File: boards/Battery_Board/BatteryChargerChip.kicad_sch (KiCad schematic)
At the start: 11 parts, among them J103 Conn_01x02, Q1 PMOS, U1 BQ25185DLHR

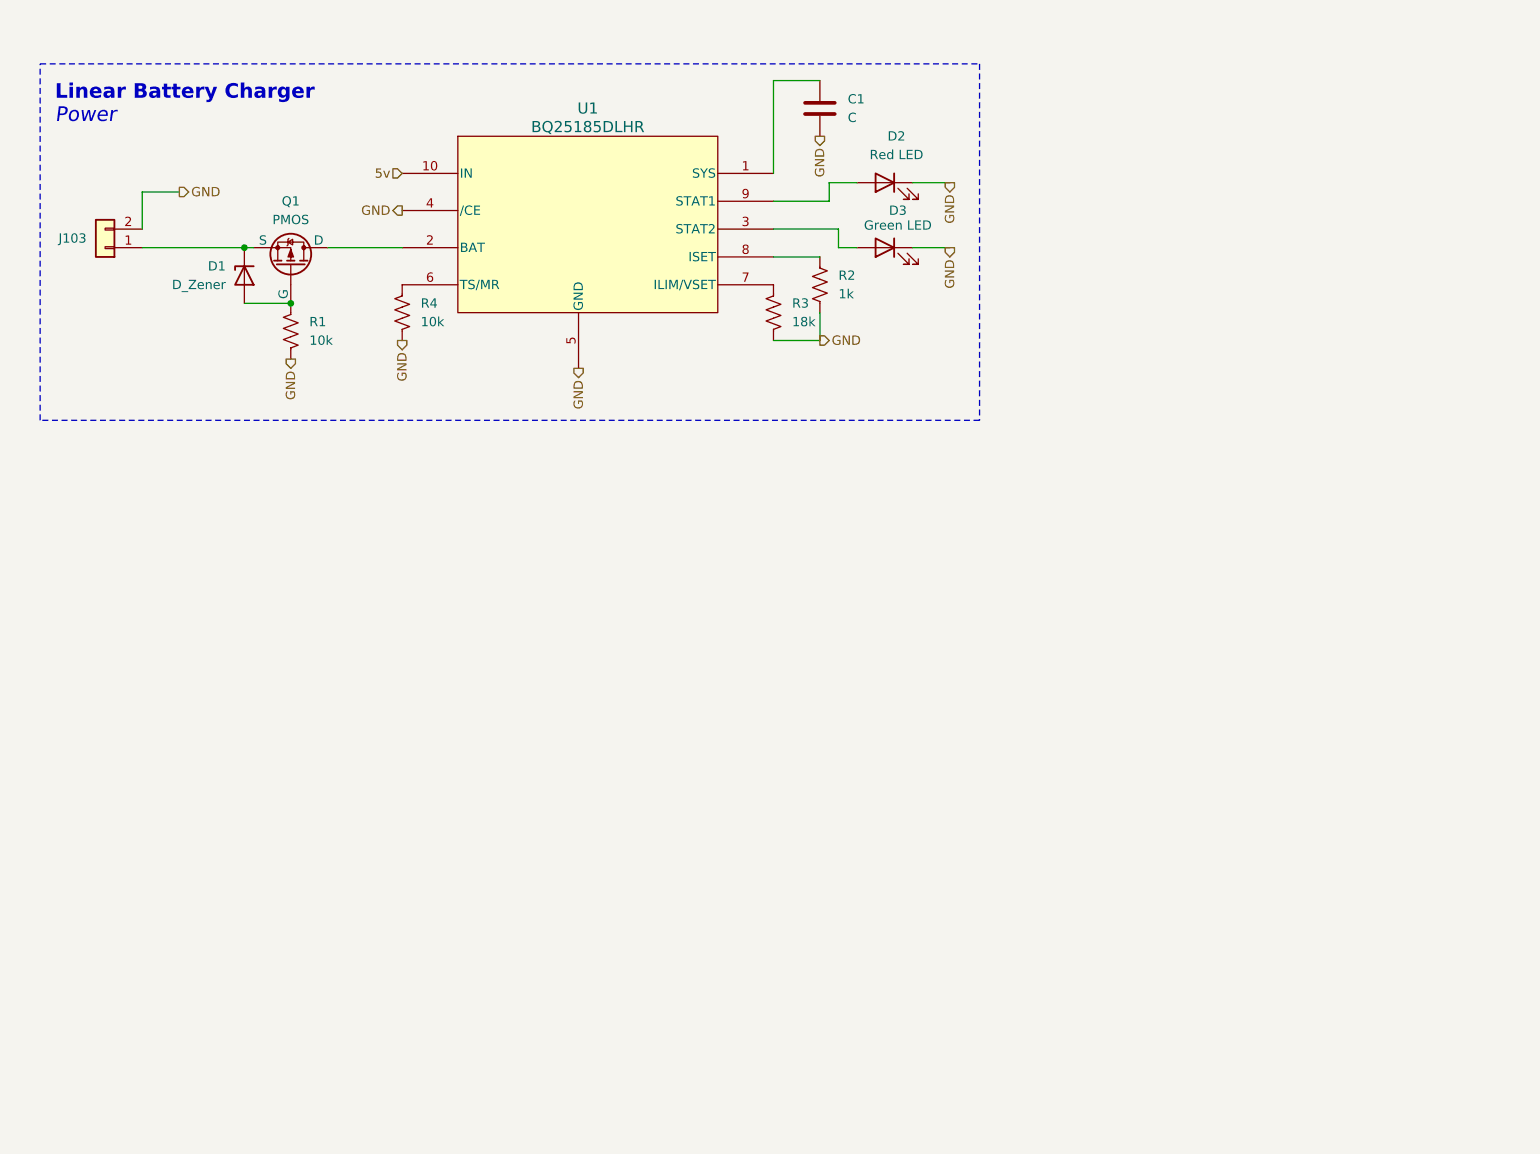
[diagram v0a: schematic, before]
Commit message: adding displays to this
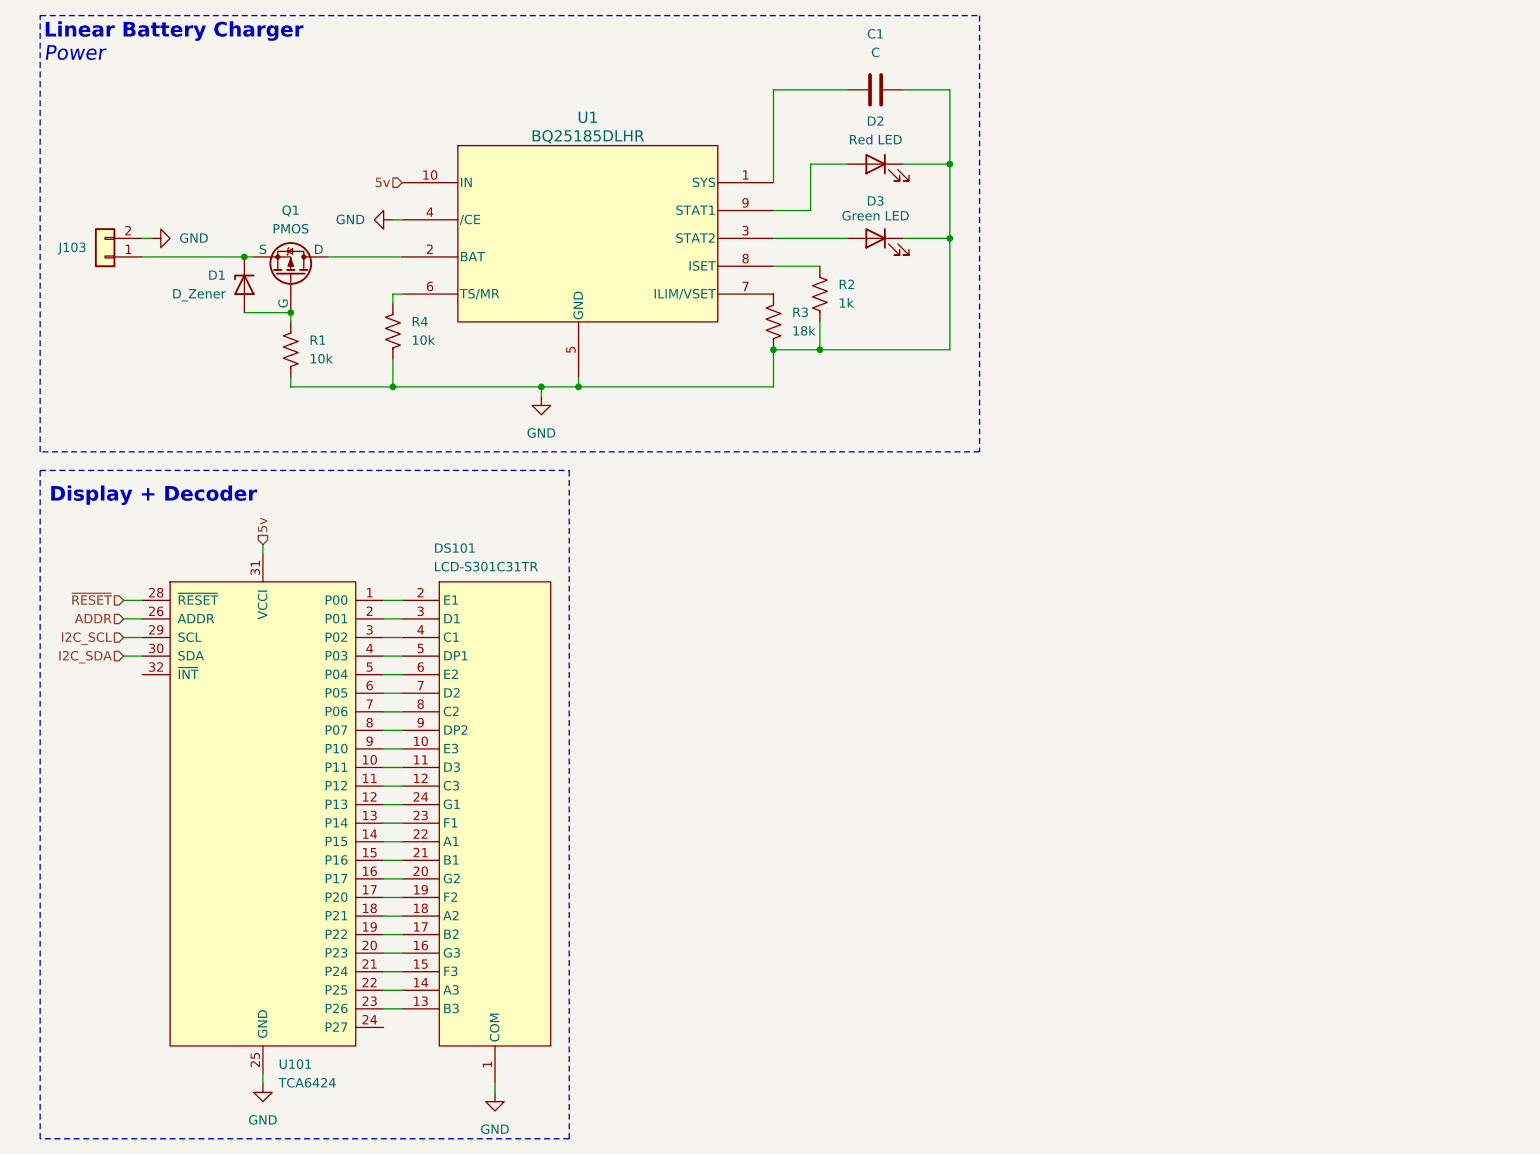
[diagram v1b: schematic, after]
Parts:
- added DS101: LCD-S301C31TR, LCD-S301C31TR, symbol Lumex_Display:LCD-S301C31TR
- added U101: TCA6424, TCA6424ARGJR:QFN50P500X500X60-33N, symbol Interface_Expander_Texas:TCA6424
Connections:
- net GND: now also DS101.1 (COM), U101.25 (GND), U101.33 (EXP)
- net 5v renamed VCCP
- net VCCP: now also U101.27 (VCCP), U101.31 (VCCI)
- new net: DS101.10 (E3), U101.9 (P10)
- new net: DS101.11 (D3), U101.10 (P11)
- new net: DS101.12 (C3), U101.11 (P12)
- new net: DS101.13 (B3), U101.23 (P26)
- new net: DS101.14 (A3), U101.22 (P25)
- new net: DS101.15 (F3), U101.21 (P24)
- new net: DS101.16 (G3), U101.20 (P23)
- new net: DS101.17 (B2), U101.19 (P22)
- new net: DS101.18 (A2), U101.18 (P21)
- new net: DS101.19 (F2), U101.17 (P20)
- new net: DS101.2 (E1), U101.1 (P00)
- new net: DS101.20 (G2), U101.16 (P17)
- new net: DS101.21 (B1), U101.15 (P16)
- new net: DS101.22 (A1), U101.14 (P15)
- new net: DS101.23 (F1), U101.13 (P14)
- new net: DS101.24 (G1), U101.12 (P13)
- new net: DS101.3 (D1), U101.2 (P01)
- new net: DS101.4 (C1), U101.3 (P02)
- new net: DS101.5 (DP1), U101.4 (P03)
- new net: DS101.6 (E2), U101.5 (P04)
- new net: DS101.7 (D2), U101.6 (P05)
- new net: DS101.8 (C2), U101.7 (P06)
- new net: DS101.9 (DP2), U101.8 (P07)
- new net ADDR: U101.26 (ADDR)
- new net I2C_SCL: U101.29 (SCL)
- new net I2C_SDA: U101.30 (SDA)
- new net ~{RESET}: U101.28 (~{RESET})
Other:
- note added: "Display + Decoder"
- moved on the sheet: C1, D1, D2, D3, J103, Q1, R1, R2, R3, R4, U1

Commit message: adding footprints, hooking up i2c busses, adding test points
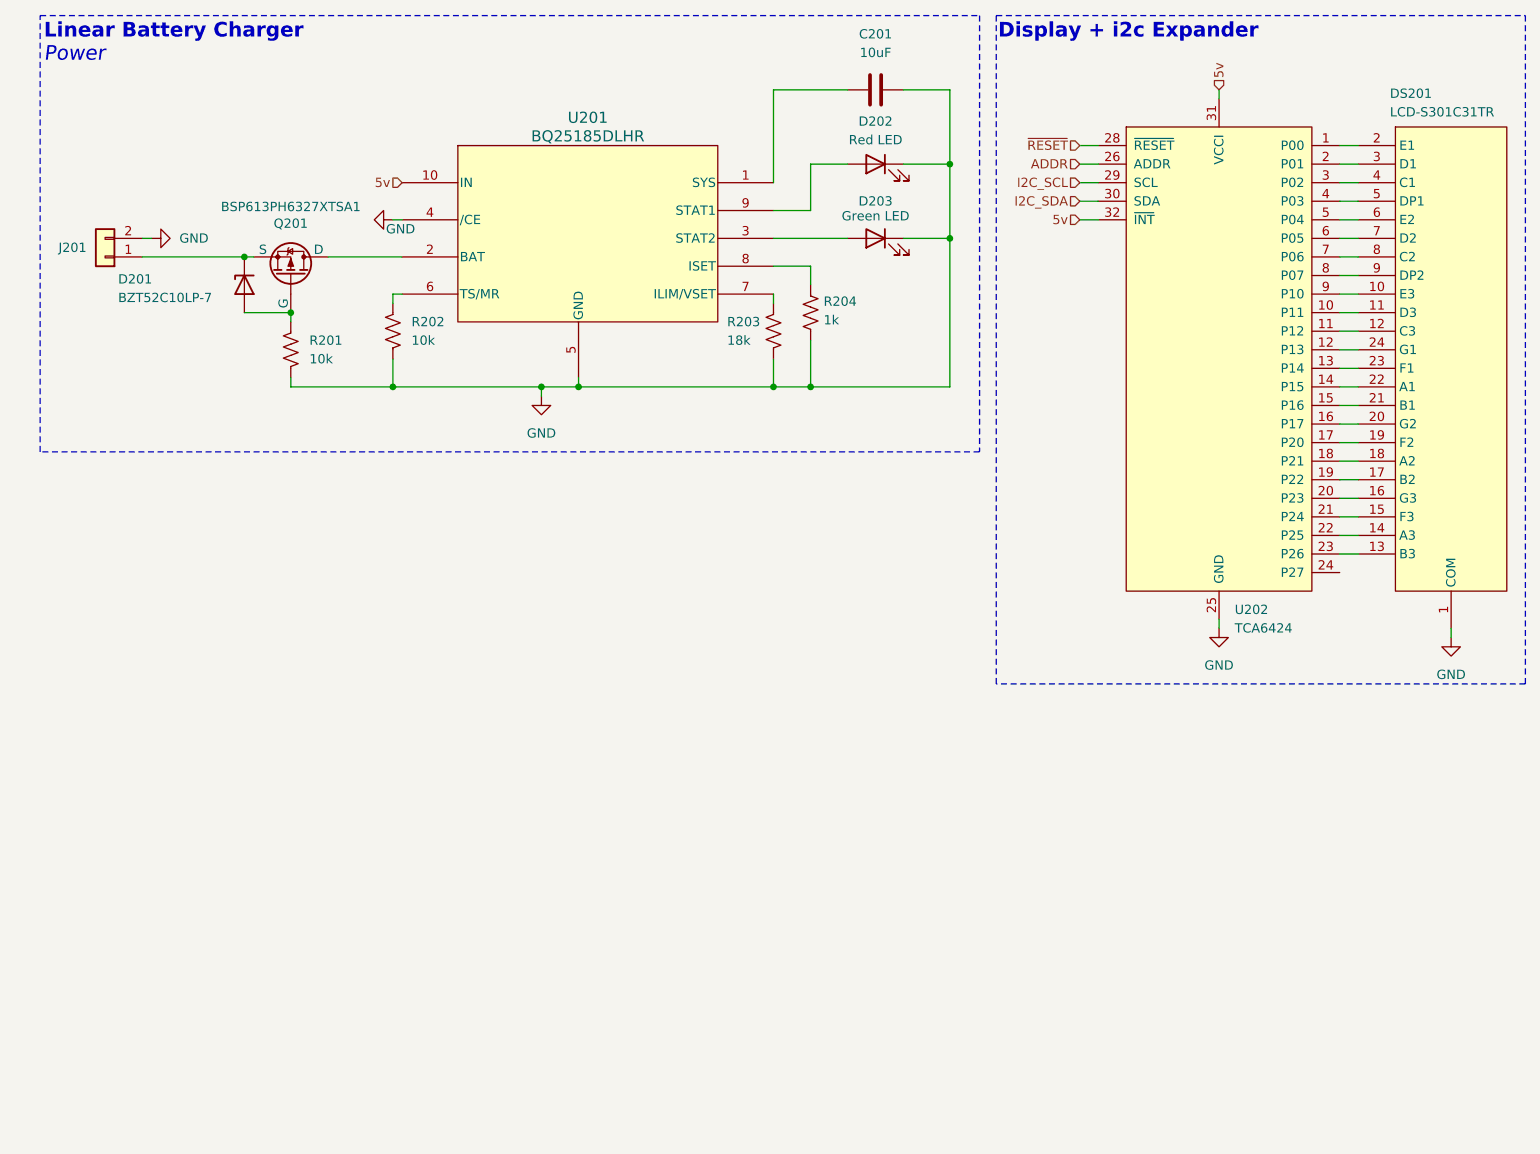
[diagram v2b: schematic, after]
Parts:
- C201: renamed from C1; value C -> 10uF; footprint (none) -> Capacitor_SMD:C_0603_1608Metric
- D201: renamed from D1; value D_Zener -> BZT52C10LP-7; footprint (none) -> Diode_SMD:D_0402_1005Metric
- D202: renamed from D2; footprint (none) -> LED_SMD:LED_0603_1608Metric
- D203: renamed from D3; footprint (none) -> LED_SMD:LED_0603_1608Metric
- DS201: renamed from DS101; footprint LCD-S301C31TR -> Lumex:LCD-S301C31TR
- Q201: renamed from Q1; value PMOS -> BSP613PH6327XTSA1; footprint (none) -> Package_TO_SOT_SMD:SOT-223
- R201: renamed from R1; footprint (none) -> Resistor_SMD:R_0603_1608Metric
- R202: renamed from R4; footprint (none) -> Resistor_SMD:R_0603_1608Metric
- R203: renamed from R3; footprint (none) -> Resistor_SMD:R_0603_1608Metric
- R204: renamed from R2; footprint (none) -> Resistor_SMD:R_0603_1608Metric
- U201: renamed from U1; footprint WSON10_DLH_TEX -> Package_DFN_QFN:Texas_DLH0010A_WSON-10-1EP_2.2x2mm_P0.4mm_EP0.9x1.5mm
- U202: renamed from U101; footprint TCA6424ARGJR:QFN50P500X500X60-33N -> Package_DFN_QFN:UQFN-32_5x5mm_P0.5mm
- renumbered J103 to J201
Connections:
- net VCCP: now also U202.32 (~{INT})
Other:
- note added: "Display + i2c Expander"
- note removed: "Display + Decoder"
- moved on the sheet: DS201, R203, R204, U202

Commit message: minor fixes, added ADC
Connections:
- net BATT_V: now reaches D201.1 (K), J201.1 (Pin_1), Q201.3 (S)
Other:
- note added: "I2C Address: x22 ADDR low, x23 ADDR high"

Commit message: fix for real this time
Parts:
- J201: footprint Connector_JST:JST_PH_B2B-PH-K_1x02_P2.00mm_Vertical -> Connector_PinHeader_1.27mm:PinHeader_1x02_P1.27mm_Vertical
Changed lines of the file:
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@@
 			)
 		)
-		(property "Footprint" "Connector_JST:JST_PH_B2B-PH-K_1x02_P2.00mm_Vertical"
+		(property "Footprint" "Connector_PinHeader_1.27mm:PinHeader_1x02_P1.27mm_Vertical"
 			(at 23.114 24.892 0)
 			(effects

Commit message: real fix this time
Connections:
- net GND: no longer U202.33 (EXP)
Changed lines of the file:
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@@
 		(pin "31"
-		)
-		(pin "33"
 		)
 		(pin "17"

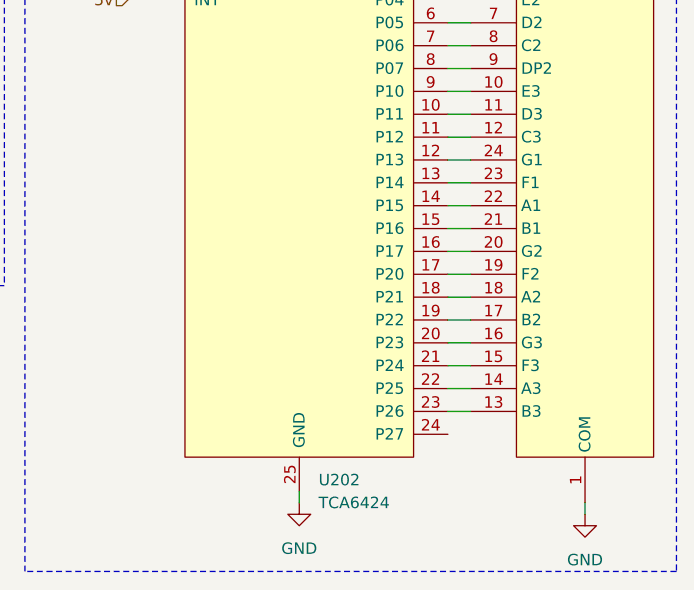
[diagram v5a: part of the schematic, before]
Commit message: changing pinouts to be more convienent
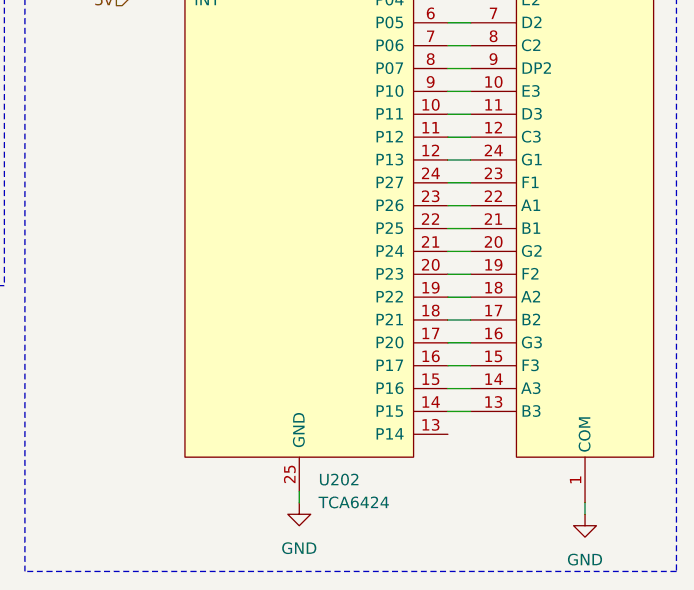
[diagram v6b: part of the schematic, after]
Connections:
- net at DS201.13 (B3): now also U202.14 (P15); no longer U202.23 (P26)
- net at DS201.14 (A3): now also U202.15 (P16); no longer U202.22 (P25)
- net at DS201.15 (F3): now also U202.16 (P17); no longer U202.21 (P24)
- net at DS201.16 (G3): now also U202.17 (P20); no longer U202.20 (P23)
- net at DS201.17 (B2): now also U202.18 (P21); no longer U202.19 (P22)
- net at DS201.18 (A2): now also U202.19 (P22); no longer U202.18 (P21)
- net at DS201.19 (F2): now also U202.20 (P23); no longer U202.17 (P20)
- net at DS201.20 (G2): now also U202.21 (P24); no longer U202.16 (P17)
- net at DS201.21 (B1): now also U202.22 (P25); no longer U202.15 (P16)
- net at DS201.22 (A1): now also U202.23 (P26); no longer U202.14 (P15)
- net at DS201.23 (F1): now also U202.24 (P27); no longer U202.13 (P14)
